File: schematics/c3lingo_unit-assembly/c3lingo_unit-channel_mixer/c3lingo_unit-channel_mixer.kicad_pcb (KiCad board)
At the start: 2 copper layers, 75 x 90 mm, 88 parts, among them J301 Interconnect, J302 PowerSupply, J303 I/O, J304 vu alt. pwr (5V), SW301 OnAir_X, SW302 Mute_X, U301 LM833-N, U302 LM339, U303 LM339, U304 LM339, U305 LM833-N

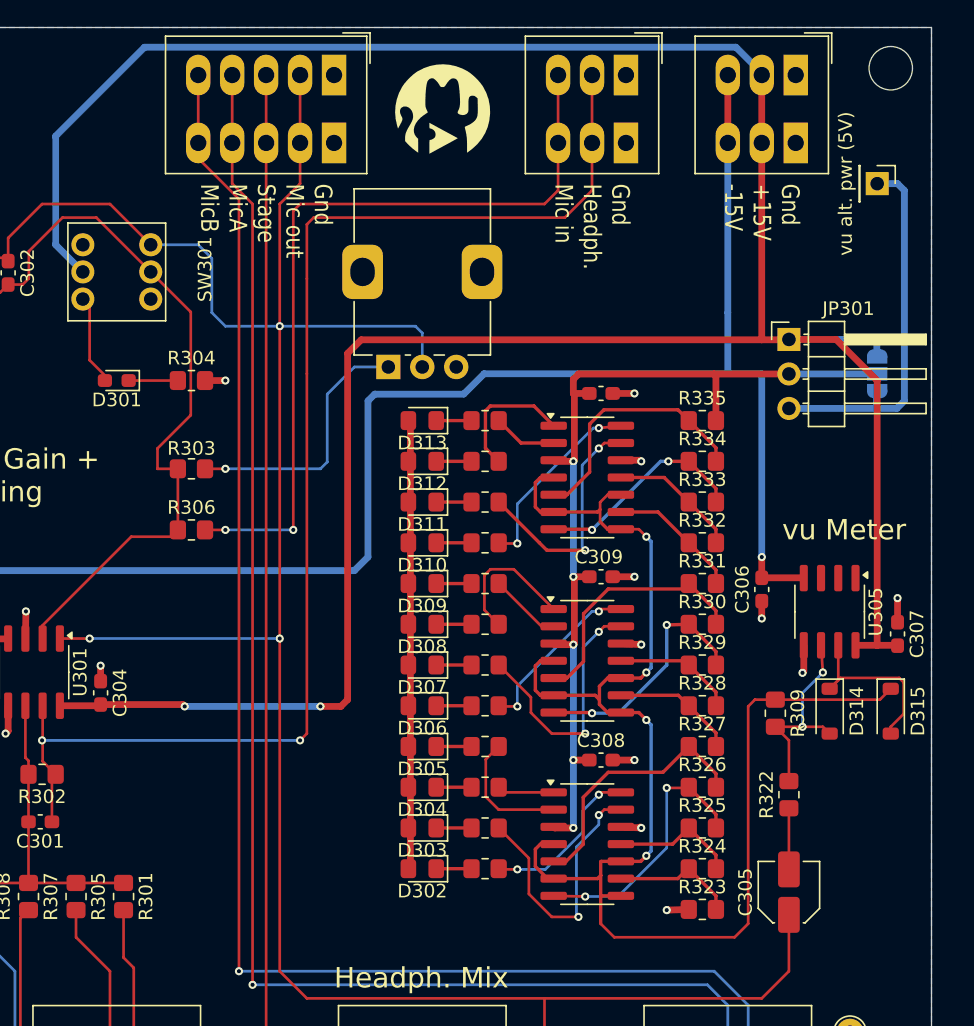
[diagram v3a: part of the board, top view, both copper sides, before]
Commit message: Channel-Mix: Rework LED supply voltage
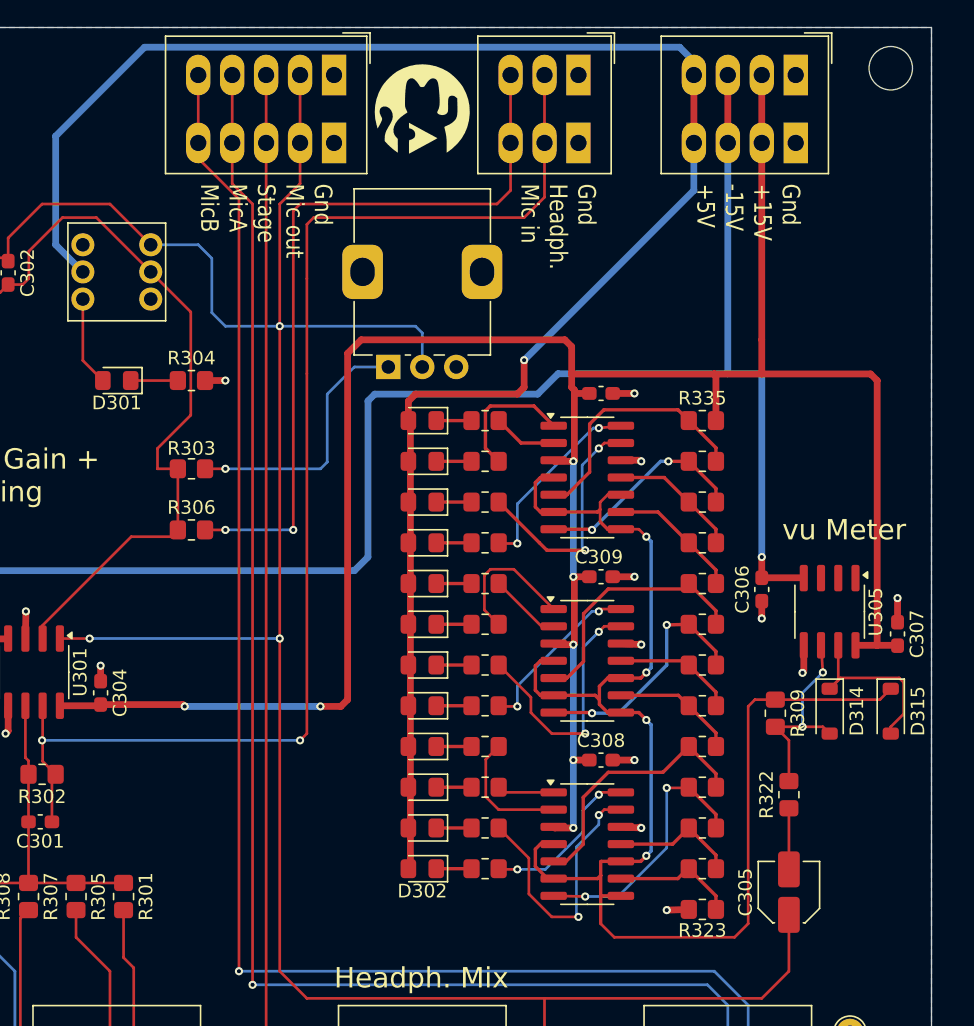
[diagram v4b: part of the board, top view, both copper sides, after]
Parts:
- removed J304: vu alt. pwr (5V), Connector_PinHeader_2.54mm:PinHeader_1x01_P2.54mm_Vertical
- removed JP301: vu PWR, Connector_PinHeader_2.54mm:PinHeader_1x03_P2.54mm_Horizontal
- removed JP302: vu PWR, Jumper:SolderJumper-3_P1.3mm_Open_RoundedPad1.0x1.5mm_NumberLabels
- D301: footprint LED_SMD:LED_0603_1608Metric_Pad1.05x0.95mm_HandSolder -> LED_SMD:LED_0805_2012Metric_Pad1.15x1.40mm_HandSolder
- J302: footprint TerminalBlock_Phoenix:TerminalBlock_Phoenix_PTSM-0,5-3-2.5-H-THR_1x03_P2.50mm_Horizontal -> TerminalBlock_Phoenix:TerminalBlock_Phoenix_PTSM-0,5-4-2.5-H-THR_1x04_P2.50mm_Horizontal
- R304, R310, R311, R312, R313, R314, R315, R319, R320, R321: value 680R -> 150R
- R316, R317, R318: value 620R -> 110R
- moved J301 3.50 mm to (99.0, 83.5)
- moved G*** 1.50 mm to (87.5, 86.0)
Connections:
- C308 pad 1: Net-(D302-A) -> +15V
- C309 pad 1: Net-(D302-A) -> +15V
- C310 pad 1: Net-(D302-A) -> +15V
- D302 pad 2: Net-(D302-A) -> +5V
- D303 pad 2: Net-(D302-A) -> +5V
- D304 pad 2: Net-(D302-A) -> +5V
- D305 pad 2: Net-(D302-A) -> +5V
- D306 pad 2: Net-(D302-A) -> +5V
- D307 pad 2: Net-(D302-A) -> +5V
- D308 pad 2: Net-(D302-A) -> +5V
- D309 pad 2: Net-(D302-A) -> +5V
- D310 pad 2: Net-(D302-A) -> +5V
- D311 pad 2: Net-(D302-A) -> +5V
- D312 pad 2: Net-(D302-A) -> +5V
- D313 pad 2: Net-(D302-A) -> +5V
- R335 pad 2: Net-(D302-A) -> +15V
- SW301 pad 5: +15V -> +5V
- U302 pad 3: Net-(D302-A) -> +15V
- U303 pad 3: Net-(D302-A) -> +15V
- U304 pad 3: Net-(D302-A) -> +15V
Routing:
- net +5V: track 27.7 -> 133.5 mm, vias 0 -> 1
- net Net-(D302-A): track 99.6 -> 0.00 mm, vias 5 -> 0
- net +15V: track 204.1 -> 178.4 mm, vias 2 -> 7
- net /MicGainIn: track 58.6 -> 55.1 mm
- net /HeadphoneMix: track 96.8 -> 93.6 mm
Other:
- board text added: "Gnd +15V -15V +5V"
- board text added: "c3lingo Interpreter Unit Channel Mixer v0.3 2024-07-07"
- board text removed: "Gnd +15V -15V"
- board text removed: "c3lingo Interpreter Unit Channel Mixer v0.3 2024-07-06"

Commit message: Channel Mixer: Fix LP filter at mic gain
1nF has about 15kHz cutoff frequency at full gain
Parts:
- C302: value 10nF -> 1nF
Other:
- board text added: "c3lingo Interpreter Unit Channel Mixer v0.3.1 2024-07-08"
- board text removed: "c3lingo Interpreter Unit Channel Mixer v0.3 2024-07-07"
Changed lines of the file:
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@@
 			)
 		)
-		(property "Value" "10nF"
+		(property "Value" "1nF"
 			(at 0 1.43 -90)
 			(layer "F.Fab")
@@
 			)
 		)
-		(property "LCSC Part #" "C57112"
+		(property "LCSC Part #" "C1588"
 			(at 0 0 -90)
 			(unlocked yes)
@@
 		(layer "Edge.Cuts")
 	)
-	(gr_text "c3lingo Interpreter Unit\nChannel Mixer\nv0.3 2024-07-07"
+	(gr_text "c3lingo Interpreter Unit\nChannel Mixer\nv0.3.1 2024-07-08"
 		(at 87.5 141.95 0)
 		(layer "B.SilkS")

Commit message: Tidy: Rename hierarchical labels
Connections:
- net /HeadphoneMix renamed /Headphone
- net /MicGainIn renamed /MicPre
- net /Monitor_OthersA renamed /Mic_OthersA
- net /Monitor_OthersB renamed /Mic_OthersB
- net /Monitor_Stage renamed /Stage
- net /PreampOut renamed /Mic_X
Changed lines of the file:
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@@
 	(net 21 "Net-(D314-K)")
 	(net 22 "Net-(D314-A)")
-	(net 23 "/Monitor_OthersB")
-	(net 24 "/Monitor_OthersA")
-	(net 25 "/Monitor_Stage")
+	(net 23 "/Mic_OthersB")
+	(net 24 "/Mic_OthersA")
+	(net 25 "/Stage")
 	(net 26 "Net-(R310-Pad2)")
 	(net 27 "Net-(R311-Pad2)")
@@
 	(net 48 "Net-(U304D-+)")
 	(net 49 "Net-(U304C-+)")
-	(net 50 "/PreampOut")
+	(net 50 "/Mic_X")
 	(net 51 "unconnected-(RV302-Pad3)")
 	(net 52 "Net-(U304B-+)")
 	(net 53 "Net-(U304A-+)")
-	(net 54 "/HeadphoneMix")
+	(net 54 "/Headphone")
 	(net 55 "unconnected-(SW301A-C-Pad3)")
-	(net 56 "/MicGainIn")
+	(net 56 "/MicPre")
 	(net 57 "Net-(R301-Pad2)")
 	(net 58 "Net-(R303-Pad1)")
@@
 			(layers "*.Cu" "*.Mask")
 			(remove_unused_layers no)
-			(net 25 "/Monitor_Stage")
+			(net 25 "/Stage")
 			(pinfunction "3")
 			(pintype "passive")
@@
 			(layers "*.Cu" "*.Mask")
 			(remove_unused_layers no)
-			(net 50 "/PreampOut")
+			(net 50 "/Mic_X")
 			(pinfunction "3")
 			(pintype "passive")
@@
 			(layers "*.Cu" "*.Mask")
 			(remove_unused_layers no)
-			(net 50 "/PreampOut")
+			(net 50 "/Mic_X")
 			(pinfunction "2")
 			(pintype "passive")
@@
 			(layers "*.Cu" "*.Mask")
 			(remove_unused_layers no)
-			(net 23 "/Monitor_OthersB")
+			(net 23 "/Mic_OthersB")
 			(pinfunction "3")
 			(pintype "passive")
@@
 			(layers "*.Cu" "*.Mask")
 			(remove_unused_layers no)
-			(net 24 "/Monitor_OthersA")
+			(net 24 "/Mic_OthersA")
 			(pinfunction "6")
 			(pintype "passive")
@@
 			(layers "*.Cu" "*.Mask")
 			(remove_unused_layers no)
-			(net 25 "/Monitor_Stage")
+			(net 25 "/Stage")
 			(pinfunction "1")
 			(pintype "passive")
@@
 			(layers "*.Cu" "*.Mask")
 			(remove_unused_layers no)
-			(net 50 "/PreampOut")
+			(net 50 "/Mic_X")
 			(pinfunction "Pin_2")
 			(pintype "passive")
@@
 			(layers "*.Cu" "*.Mask")
 			(remove_unused_layers no)
-			(net 50 "/PreampOut")
+			(net 50 "/Mic_X")
 			(pinfunction "Pin_2")
 			(pintype "passive")
@@
 			(layers "*.Cu" "*.Mask")
 			(remove_unused_layers no)
-			(net 25 "/Monitor_Stage")
+			(net 25 "/Stage")
 			(pinfunction "Pin_3")
 			(pintype "passive")
@@
 			(layers "*.Cu" "*.Mask")
 			(remove_unused_layers no)
-			(net 25 "/Monitor_Stage")
+			(net 25 "/Stage")
 			(pinfunction "Pin_3")
 			(pintype "passive")
@@
 			(layers "*.Cu" "*.Mask")
 			(remove_unused_layers no)
-			(net 24 "/Monitor_OthersA")
+			(net 24 "/Mic_OthersA")
 			(pinfunction "Pin_4")
 			(pintype "passive")
@@
 			(layers "*.Cu" "*.Mask")
 			(remove_unused_layers no)
-			(net 24 "/Monitor_OthersA")
+			(net 24 "/Mic_OthersA")
 			(pinfunction "Pin_4")
 			(pintype "passive")
@@
 			(layers "*.Cu" "*.Mask")
 			(remove_unused_layers no)
-			(net 23 "/Monitor_OthersB")
+			(net 23 "/Mic_OthersB")
 			(pinfunction "Pin_5")
 			(pintype "passive")
@@
 			(layers "*.Cu" "*.Mask")
 			(remove_unused_layers no)
-			(net 23 "/Monitor_OthersB")
+			(net 23 "/Mic_OthersB")
 			(pinfunction "Pin_5")
 			(pintype "passive")
@@
 			(layers "*.Cu" "*.Mask")
 			(remove_unused_layers no)
-			(net 50 "/PreampOut")
+			(net 50 "/Mic_X")
 			(pinfunction "A")
 			(pintype "passive")
@@
 			(layers "*.Cu" "*.Mask")
 			(remove_unused_layers no)
-			(net 24 "/Monitor_OthersA")
+			(net 24 "/Mic_OthersA")
 			(pinfunction "1")
 			(pintype "passive")
@@
 			(layers "*.Cu" "*.Mask")
 			(remove_unused_layers no)
-			(net 50 "/PreampOut")
+			(net 50 "/Mic_X")
 			(pinfunction "2")
 			(pintype "passive")
@@
 			(layers "F.Cu" "F.Paste" "F.Mask")
 			(roundrect_rratio 0.25)
-			(net 50 "/PreampOut")
+			(net 50 "/Mic_X")
 			(pintype "passive")
 		)
@@
 			(layers "*.Cu" "*.Mask")
 			(remove_unused_layers no)
-			(net 50 "/PreampOut")
+			(net 50 "/Mic_X")
 			(pinfunction "1")
 			(pintype "passive")
@@
 			(layers "F.Cu" "F.Paste" "F.Mask")
 			(roundrect_rratio 0.208333)
-			(net 54 "/HeadphoneMix")
+			(net 54 "/Headphone")
 			(pintype "passive")
 		)
@@
 			(layers "F.Cu" "F.Paste" "F.Mask")
 			(roundrect_rratio 0.208333)
-			(net 56 "/MicGainIn")
+			(net 56 "/MicPre")
 			(pintype "passive")
 		)
@@
 			(layers "F.Cu" "F.Paste" "F.Mask")
 			(roundrect_rratio 0.15625)
-			(net 50 "/PreampOut")
+			(net 50 "/Mic_X")
 			(pintype "passive")
 		)
@@
 			(layers "*.Cu" "*.Mask")
 			(remove_unused_layers no)
-			(net 23 "/Monitor_OthersB")
+			(net 23 "/Mic_OthersB")
 			(pinfunction "1")
 			(pintype "passive")
@@
 			(layers "F.Cu" "F.Paste" "F.Mask")
 			(roundrect_rratio 0.25)
-			(net 54 "/HeadphoneMix")
+			(net 54 "/Headphone")
 			(pintype "passive")
 		)
@@
 			(layers "F.Cu" "F.Paste" "F.Mask")
 			(roundrect_rratio 0.25)
-			(net 50 "/PreampOut")
+			(net 50 "/Mic_X")
 			(pintype "output")
 		)
@@
 			(layers "F.Cu" "F.Paste" "F.Mask")
 			(roundrect_rratio 0.25)
-			(net 54 "/HeadphoneMix")
+			(net 54 "/Headphone")
 			(pintype "output")
 		)
@@
 			(layers "*.Cu" "*.Mask")
 			(remove_unused_layers no)
-			(net 54 "/HeadphoneMix")
+			(net 54 "/Headphone")
 			(pinfunction "Pin_2")
 			(pintype "passive")
@@
 			(layers "*.Cu" "*.Mask")
 			(remove_unused_layers no)
-			(net 54 "/HeadphoneMix")
+			(net 54 "/Headphone")
 			(pinfunction "Pin_2")
 			(pintype "passive")
@@
 			(layers "*.Cu" "*.Mask")
 			(remove_unused_layers no)
-			(net 56 "/MicGainIn")
+			(net 56 "/MicPre")
 			(pinfunction "Pin_3")
 			(pintype "passive")
@@
 			(layers "*.Cu" "*.Mask")
 			(remove_unused_layers no)
-			(net 56 "/MicGainIn")
+			(net 56 "/MicPre")
 			(pinfunction "Pin_3")
 			(pintype "passive")

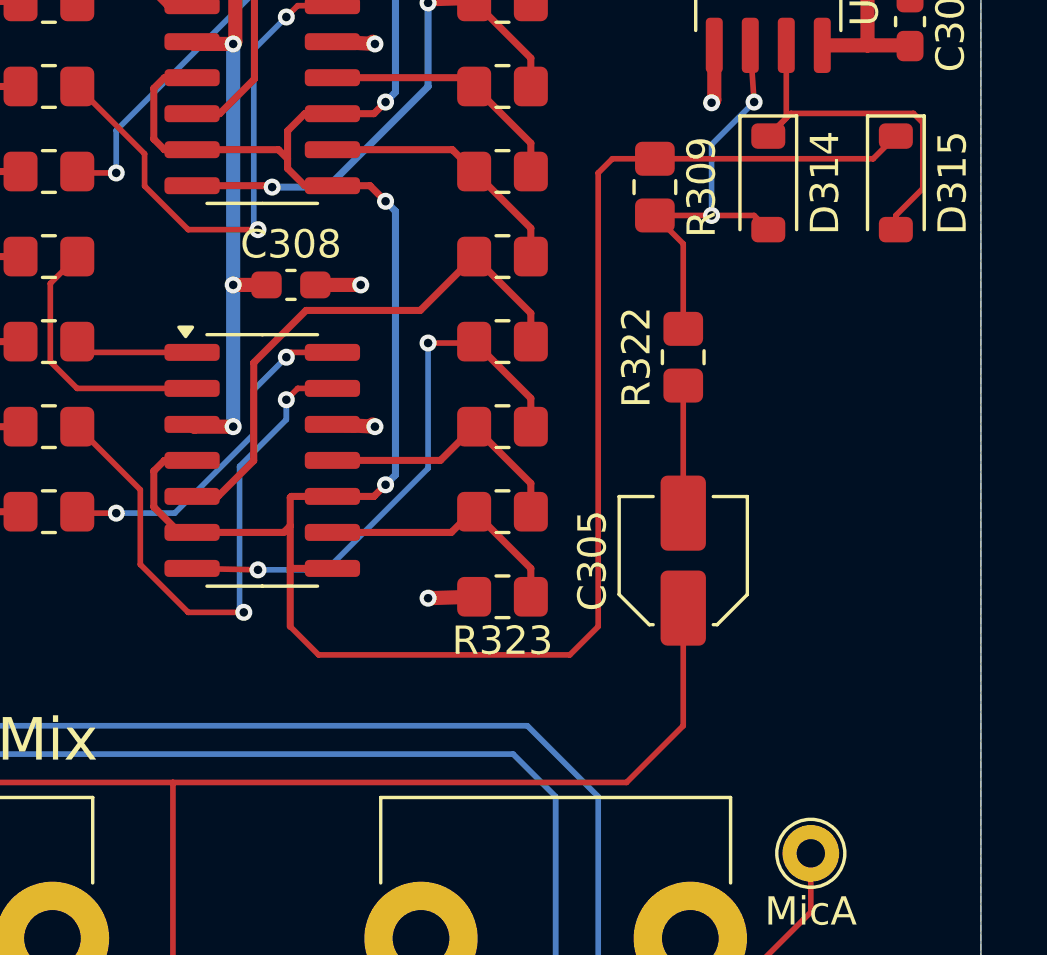
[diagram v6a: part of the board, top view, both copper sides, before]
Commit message: Channel Mixer: Add LP filter to V/U meter
Note: schematic and dimenstions PDFs not updated as more changes come

To reduce HF noise on the power rail introduced by the switching of the comperators
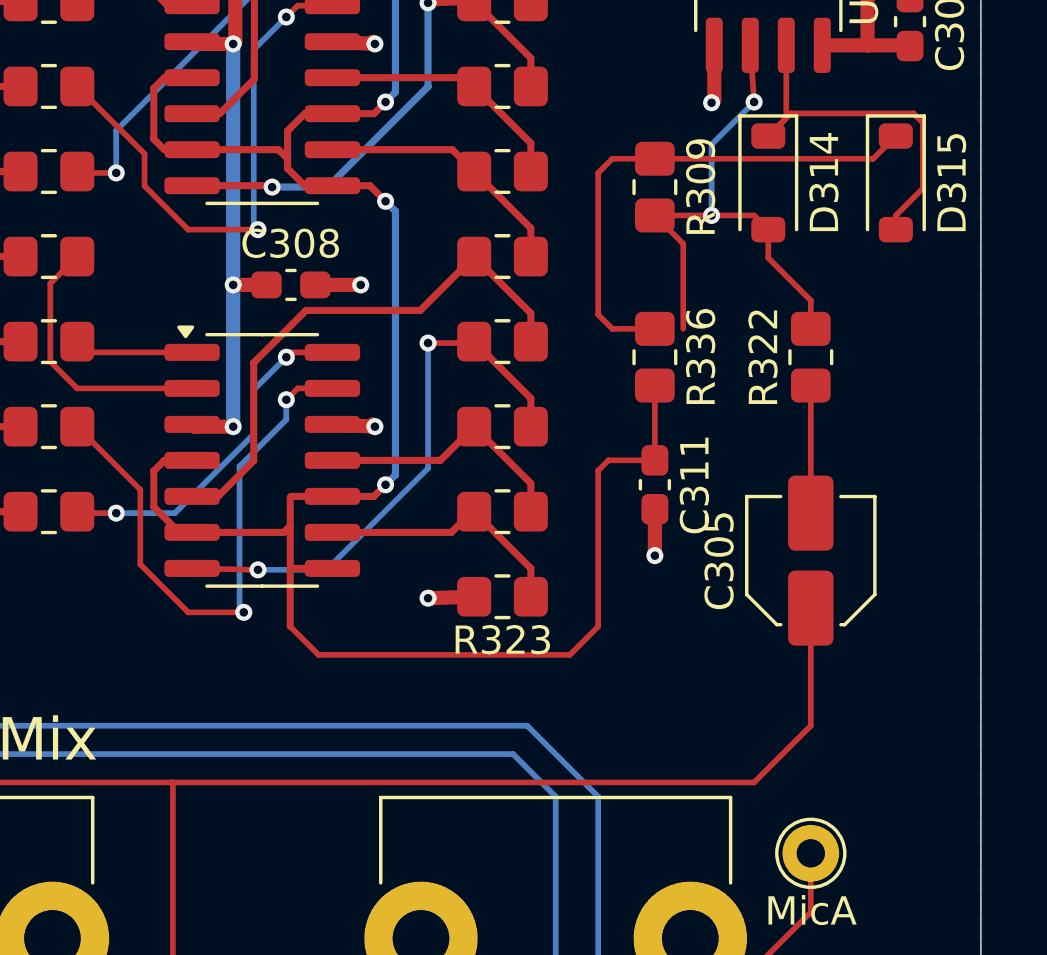
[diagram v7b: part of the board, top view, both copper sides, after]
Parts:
- added C311: 100nF, Capacitor_SMD:C_0603_1608Metric_Pad1.08x0.95mm_HandSolder, F.Cu at (113.5, 141.0)
- added R336: 100K, Resistor_SMD:R_0805_2012Metric_Pad1.20x1.40mm_HandSolder, F.Cu at (113.5, 136.5)
- moved C305 4.50 mm to (119.0, 143.7)
- moved R322 4.50 mm to (119.0, 136.5)
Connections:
- U302 pad 10: Net-(D315-K) -> Net-(U302A--)
- U302 pad 4: Net-(D315-K) -> Net-(U302A--)
- U302 pad 6: Net-(D315-K) -> Net-(U302A--)
- U302 pad 8: Net-(D315-K) -> Net-(U302A--)
- U303 pad 10: Net-(D315-K) -> Net-(U302A--)
- U303 pad 4: Net-(D315-K) -> Net-(U302A--)
- U303 pad 6: Net-(D315-K) -> Net-(U302A--)
- U303 pad 8: Net-(D315-K) -> Net-(U302A--)
- U304 pad 10: Net-(D315-K) -> Net-(U302A--)
- U304 pad 4: Net-(D315-K) -> Net-(U302A--)
- U304 pad 6: Net-(D315-K) -> Net-(U302A--)
- U304 pad 8: Net-(D315-K) -> Net-(U302A--)
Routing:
- net Net-(U302A--): track 0.00 -> 93.0 mm, vias 0 -> 4
- net Net-(D315-K): track 109.7 -> 18.2 mm, vias 4 -> 0
- net /Mic_X: track 188.0 -> 192.5 mm
- net Net-(D314-A): track 15.4 -> 19.6 mm
- net GND: track 23.9 -> 25.6 mm, vias 15 -> 16
